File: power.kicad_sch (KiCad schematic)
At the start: 4 parts, among them U8 INA187A1IDBVR

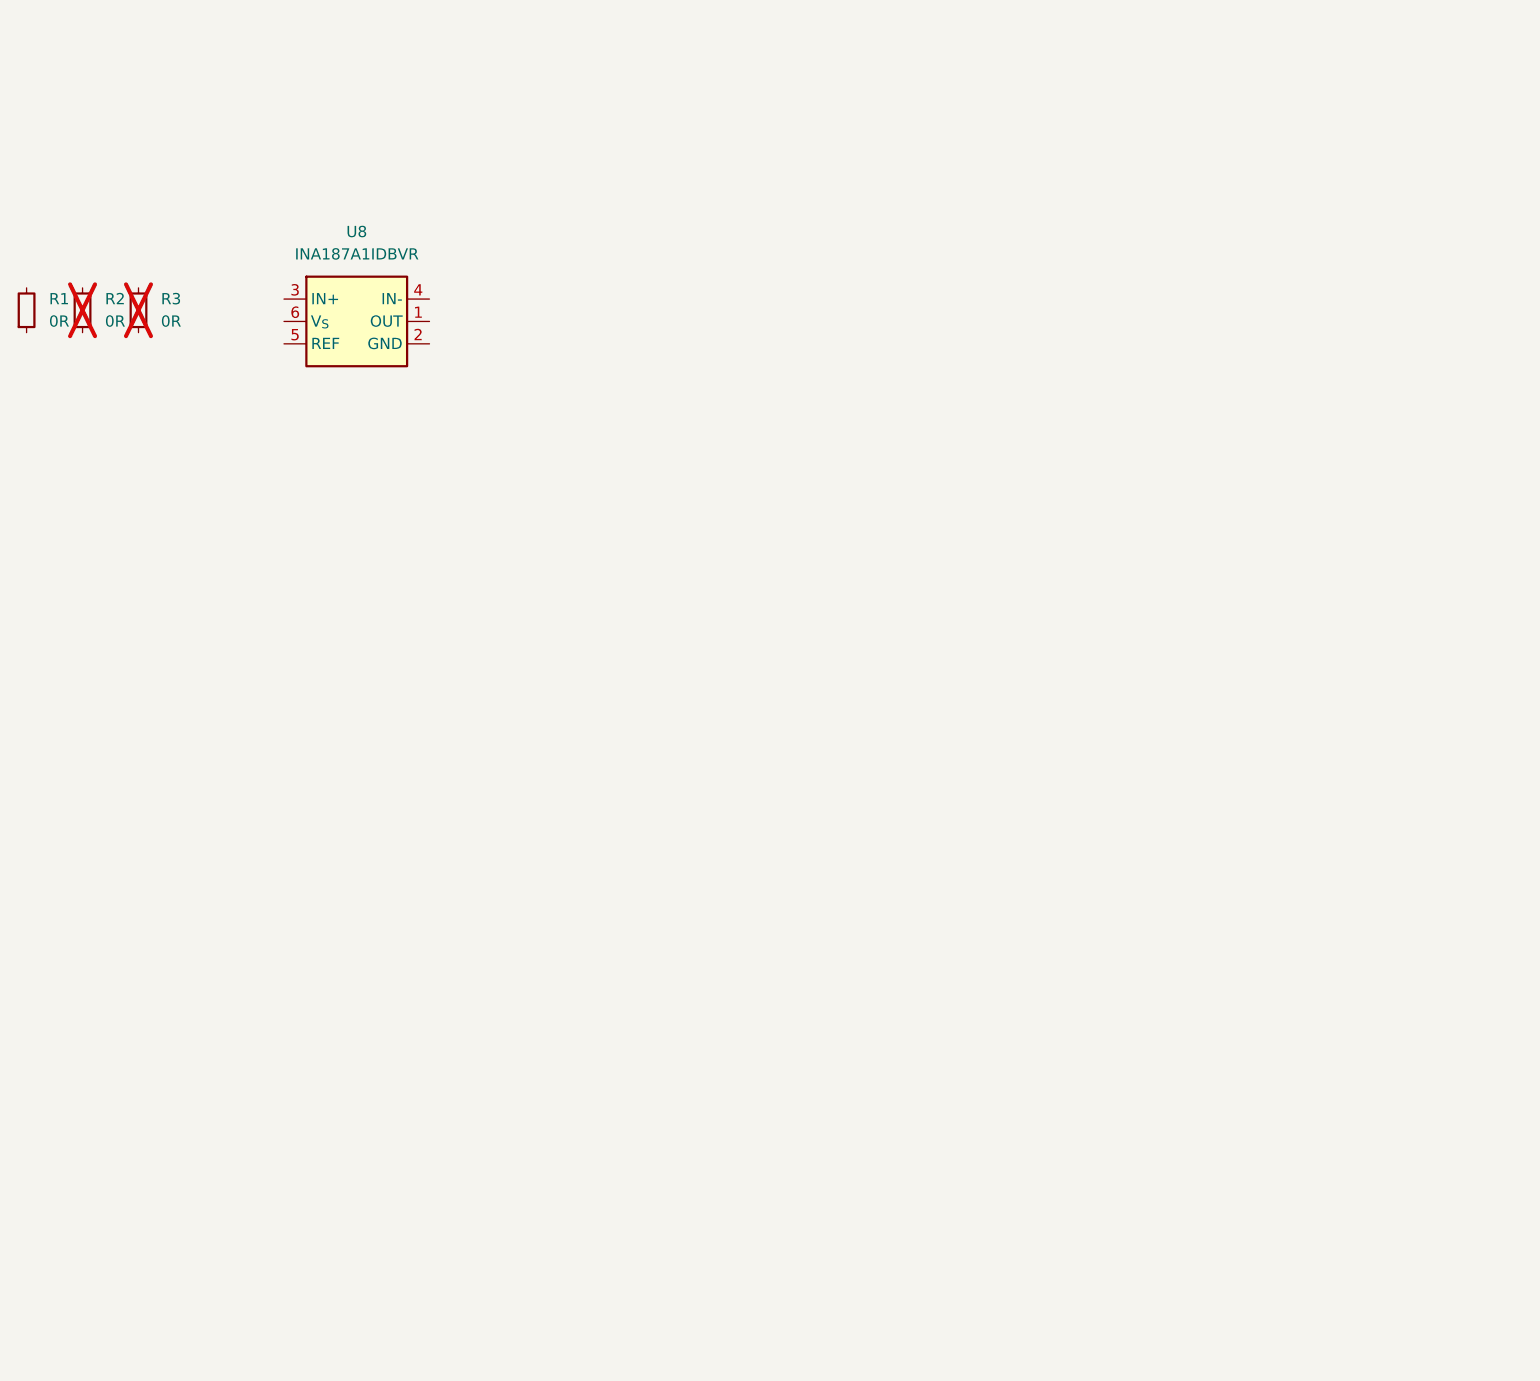
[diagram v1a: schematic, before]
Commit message: [#94728] Add current measurement and DCDC converter
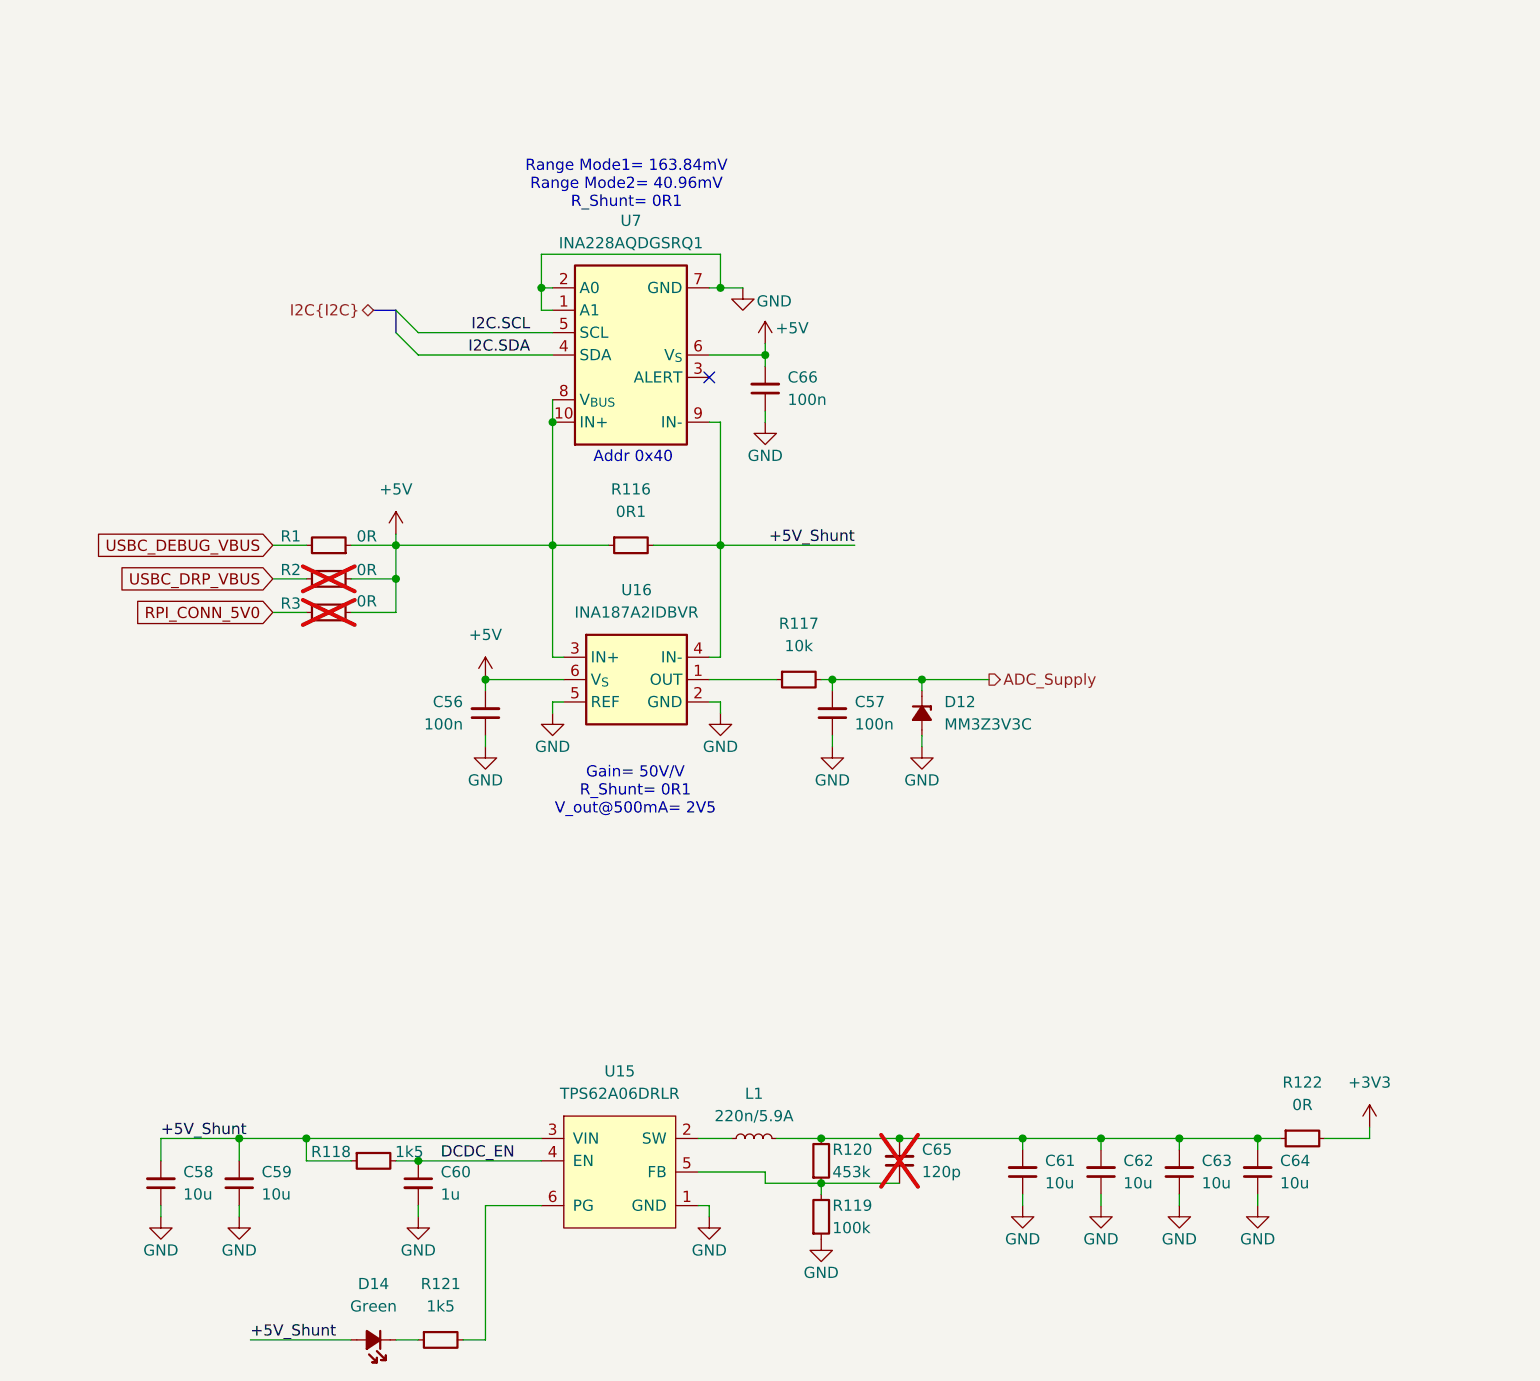
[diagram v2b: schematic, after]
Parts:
- removed U8: INA187A1IDBVR, antmicro-footprints:SOT-23-6, symbol antmicroPowerMeasurement:INA187A1IDBVR
- added C56, C57, C66: C_100n_0402, antmicro-footprints:C_0402_1005Metric, symbol antmicroCapacitors0402:C_100n_0402
- added C58, C59, C61, C62, C63, C64: C_10u_0402, antmicro-footprints:C_0402_1005Metric, symbol antmicroCapacitors0402:C_10u_0402
- added C60: C_1u_0402, antmicro-footprints:C_0402_1005Metric, symbol antmicroCapacitors0402:C_1u_0402
- added C65: C_120p_100V_0402, antmicro-footprints:C_0402_1005Metric, symbol antmicroCapacitors0402:C_120p_100V_0402
- added D12: MM3Z3V3C, antmicro-footprints:D_SOD-323F, symbol antmicroDiodesZenerSingle:MM3Z3V3C
- added D14: LED_G_0603_LTST-C190GKT, antmicro-footprints:LED_0603_1608Metric_G, symbol antmicroLEDIndicationDiscrete:LED_G_0603_LTST-C190GKT
- added L1: L_220n_5.9A_1008, antmicro-footprints:L_1008_2520Metric, symbol antmicroFixedInductors:L_220n_5.9A_1008
- added R116: R_0R1_0805, antmicro-footprints:R_0805_2012Metric, symbol antmicroResistorsmisc:R_0R1_0805
- added R117: R_10k_0402, antmicro-footprints:R_0402_1005Metric, symbol antmicroResistors0402:R_10k_0402
- added R118, R121: R_1k5_0402, antmicro-footprints:R_0402_1005Metric, symbol antmicroResistors0402:R_1k5_0402
- added R119: R_100k_0.1%_0402, antmicro-footprints:R_0402_1005Metric, symbol antmicroResistors0402:R_100k_0.1%_0402
- added R120: R_453k_0402, antmicro-footprints:R_0402_1005Metric, symbol antmicroResistors0402:R_453k_0402
- added R122: R_0R_0402, antmicro-footprints:R_0402_1005Metric, symbol antmicroResistors0402:R_0R_0402
- added U15: TPS62A06DRLR, antmicro-footprints:SOT-563, symbol antmicroDCDCConverters:TPS62A06DRLR
- added U16: INA187A2IDBVR, antmicro-footprints:SOT-23-6, symbol antmicroPowerMeasurement:INA187A2IDBVR
- added U7: INA228AQDGSRQ1, antmicro-footprints:VSSOP-10_3x3mm_P0.5mm, symbol antmicroPowerMeasurement:INA228AQDGSRQ1
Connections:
- net +5V: now reaches R2.1
- net +5V: now also R1.1, R3.1, C56.2, C66.2, R116.1, U16.3 (IN+), U16.6 (V_{S}), U7.10 (IN+), U7.6 (V_{S}), U7.8 (V_{BUS})
- net USBC_DRP_VBUS: now reaches R2.2
- net USBC_DEBUG_VBUS: now reaches R1.2
- net RPI_CONN_5V0: now reaches R3.2
- new net: R117.1, U16.1 (OUT)
- new net: C61.2, C62.2, C63.2, C64.2, C65.2, L1.2, R120.2, R122.1
- new net: C65.1, R119.2, R120.1, U15.5 (FB)
- new net: D14.1 (C), R121.1
- new net: R121.2, U15.6 (PG)
- new net: L1.1, U15.2 (SW)
- new net +3V3: R122.2
- new net +5V_Shunt: C58.2, C59.2, D14.2 (A), R116.2, R118.1, U15.3 (VIN), U16.4 (IN-), U7.9 (IN-)
- new net ADC_Supply: C57.2, D12.1 (C), R117.2
- new net DCDC_EN: C60.1, R118.2, U15.4 (EN)
- new net GND: C56.1, C57.1, C58.1, C59.1, C60.2, C61.1, C62.1, C63.1, C64.1, C66.1, D12.2 (A), R119.1, U15.1 (GND), U16.2 (GND), U16.5 (REF), U7.1 (A1), U7.2 (A0), U7.7 (GND)
- new net I2C.SCL: U7.5 (SCL)
- new net I2C.SDA: U7.4 (SDA)
- no-connect marks 0 -> 1
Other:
- note added: "Addr 0x40"
- note added: "Gain= 50V/V R_Shunt= 0R1 V_out@500mA= 2V5"
- note added: "Range Mode1= 163.84mV Range Mode2= 40.96mV R_Shunt= 0R1"
- moved on the sheet: R1, R2, R3

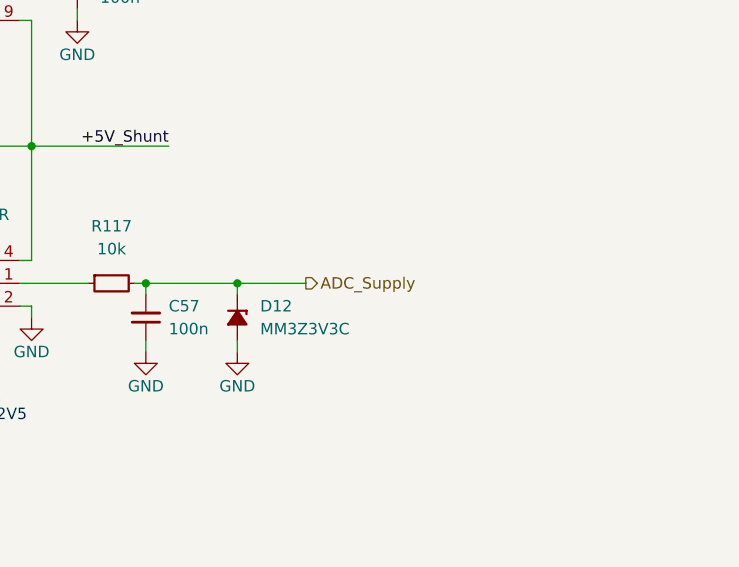
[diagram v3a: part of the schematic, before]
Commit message: [#95036] Reconnect IMU interupts
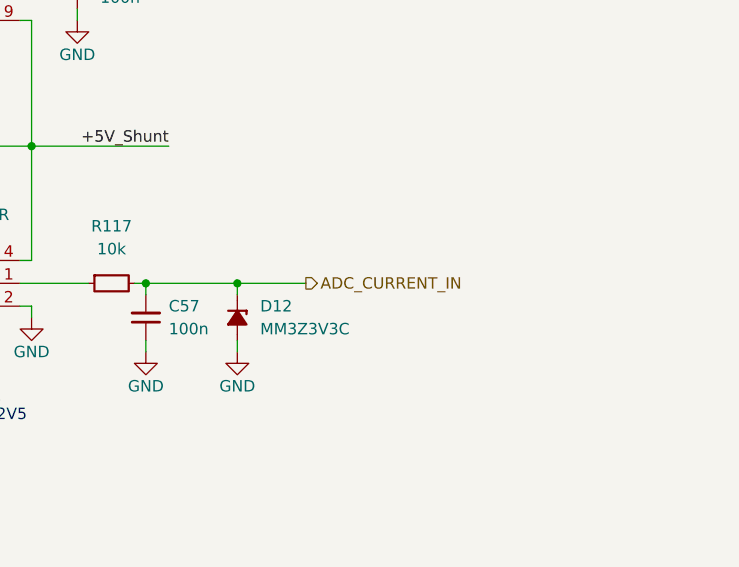
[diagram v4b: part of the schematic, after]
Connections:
- net ADC_Supply renamed ADC_CURRENT_IN
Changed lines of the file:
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@@
 		)
 	)
-	(hierarchical_label "ADC_Supply"
+	(hierarchical_label "ADC_CURRENT_IN"
 		(shape output)
 		(at 223.52 125.73 0)

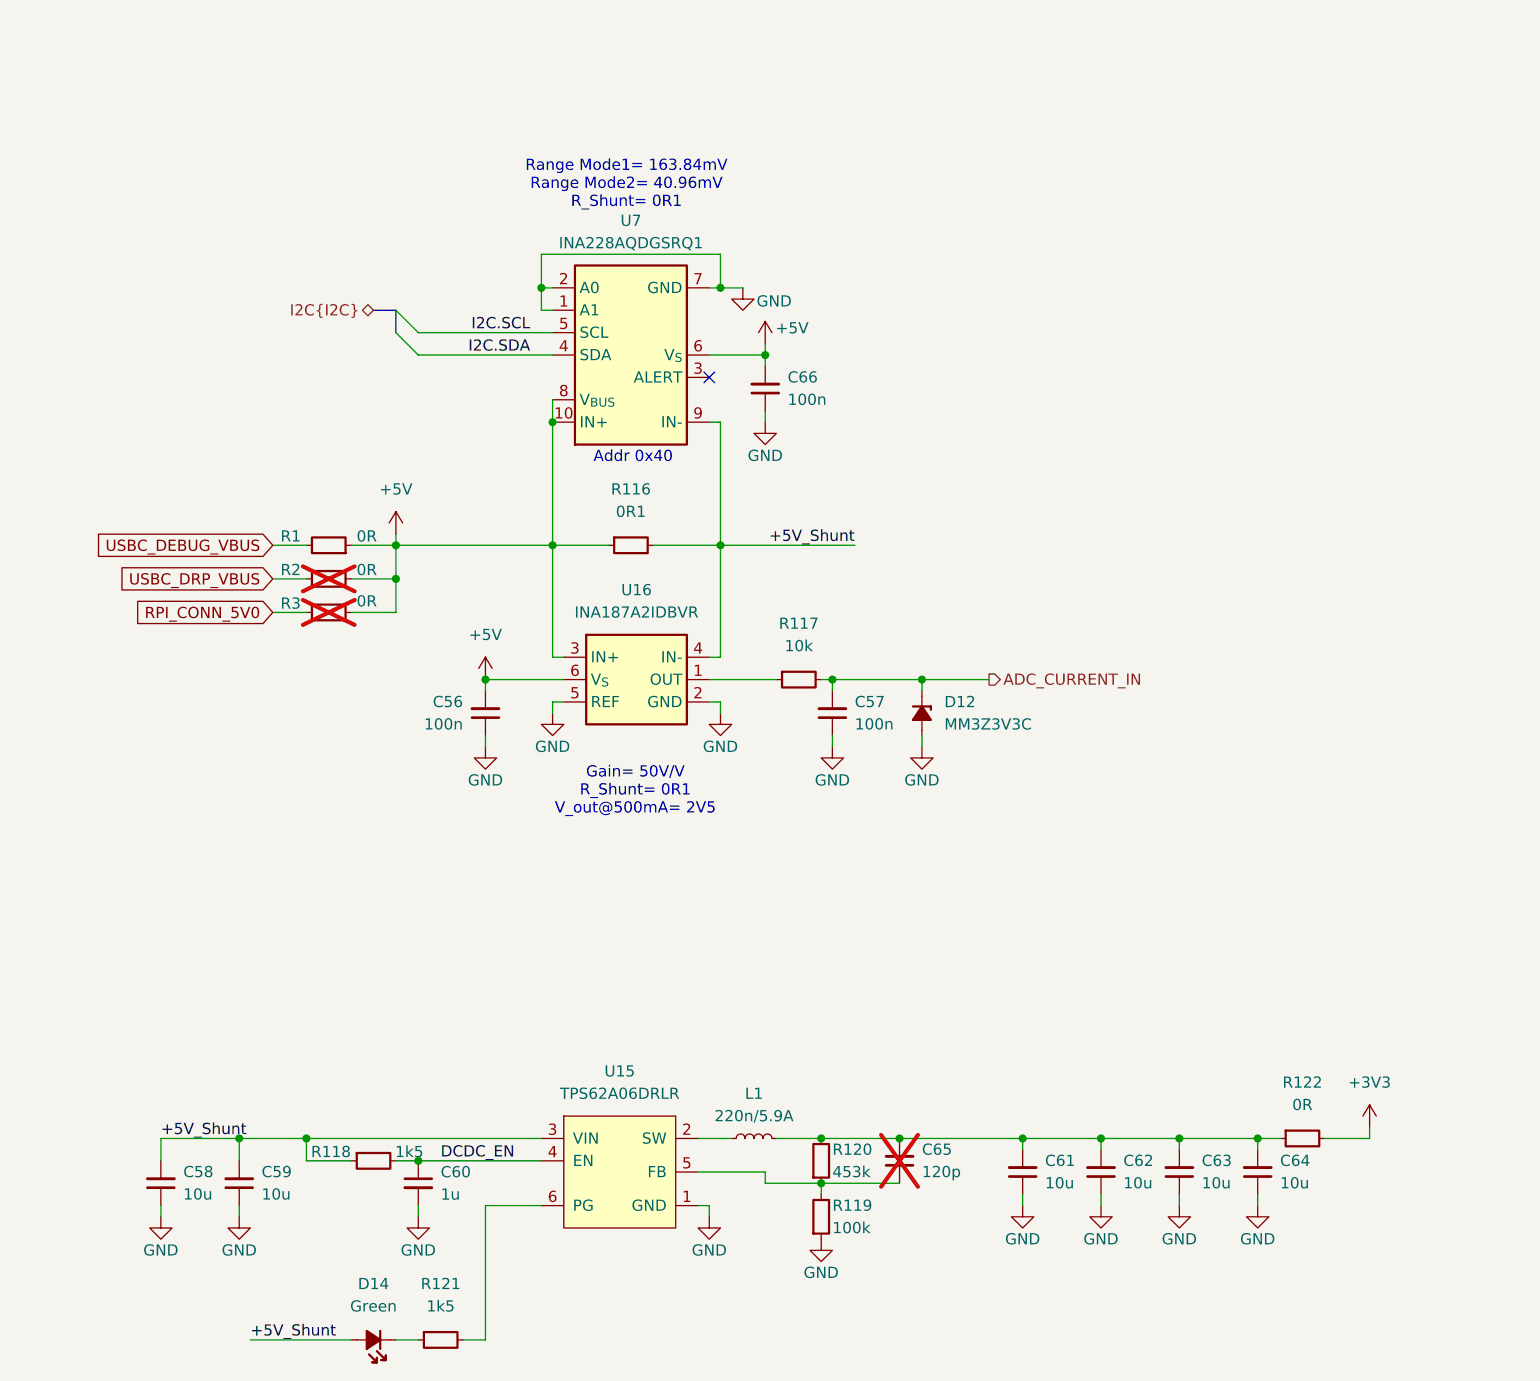
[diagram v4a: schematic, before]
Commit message: [#95036] Add CAN bus subsheet
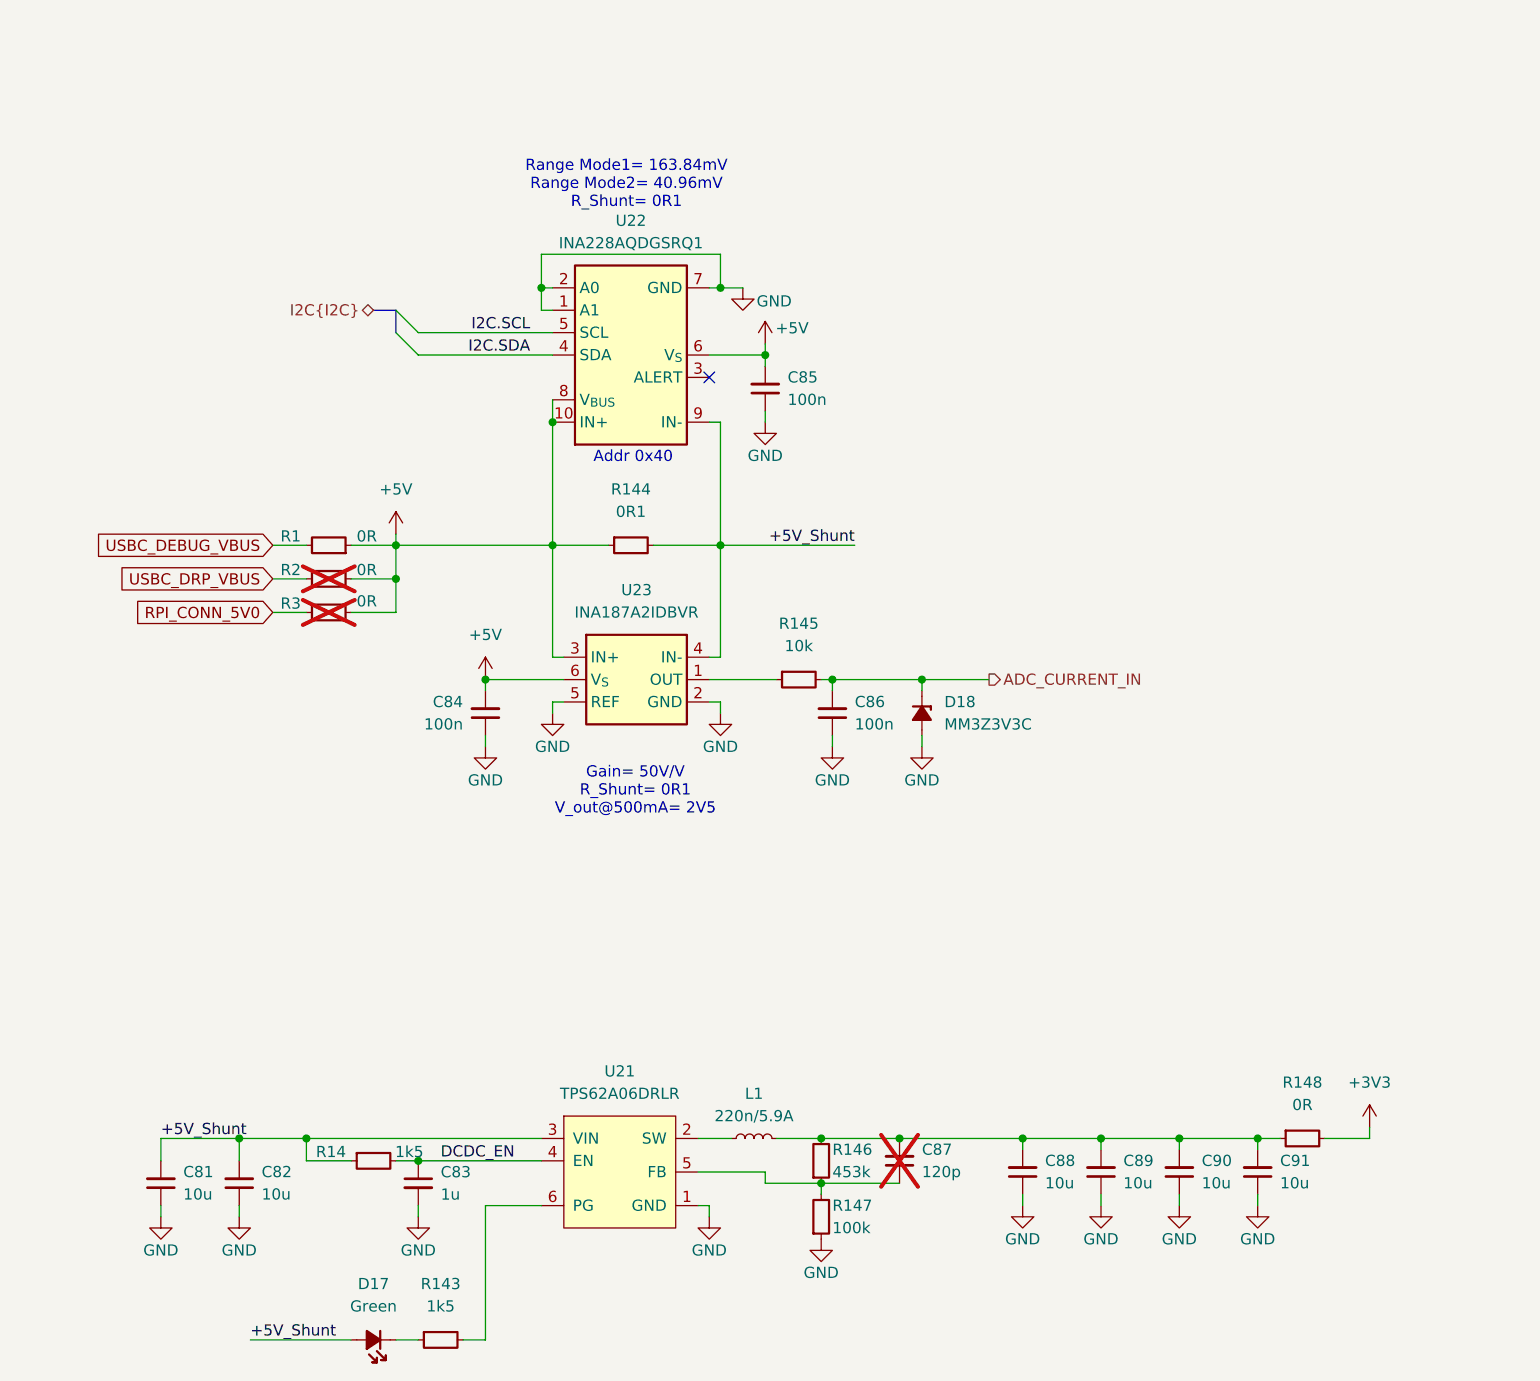
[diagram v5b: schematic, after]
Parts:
- renumbered C58 to C81, C59 to C82, C60 to C83, C56 to C84, C66 to C85, C57 to C86, C65 to C87, C61 to C88, C62 to C89, C63 to C90, C64 to C91, D14 to D17, D12 to D18, R118 to R14, R121 to R143, R116 to R144, R117 to R145, R120 to R146, R119 to R147, R122 to R148, U15 to U21, U7 to U22, U16 to U23
